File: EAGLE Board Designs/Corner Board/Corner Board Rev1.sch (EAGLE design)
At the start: 15 parts, among them J1 CONNECTOR-4_μF_T_V_BLACK, J2 CONNECTOR-2_MOLEX_NANOFIT_PTH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, J3 CONNECTOR-10_MF_T_V_, J4 CONNECTOR-4_μF_T_V_BLACK, J5 CONNECTOR-4_μF_T_V_BLACK, U1 VOLTAGE_REGULATOR_SOT-89_15V, U2 OPAMP_1_CHANNEL_OPA991, U3 INA823DT

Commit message: Update Corner Board Rev1.sch
Added MAX6176 part to Corner Board Rev1 schematic.
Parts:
- removed R3, R5: RESISTOR_0603_2K, HyTechDevices:RESISTOR_0603_2K
- added C3: CAPACITOR_0603_25V_1UF, HyTechDevices:CAPACITOR_0603_25V_1UF
- added U$6: VOLTAGE_REFERENCE__10V, temp:VOLTAGE_REFERENCE__10V
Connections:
- new net OUT: C3.1, U$6.OUT
- net +24V: now also U$6.VIN
- net GND: now also C3.2, U$6.GND
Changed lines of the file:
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@@
 <part name="P5" library="HyTechSupplies" deviceset="GND" device=""/>
 <part name="U2" library="HyTechDevices" deviceset="OPAMP_1_CHANNEL_*" device="" technology="OPA991"/>
-<part name="U$3" library="HyTechSupplies" deviceset="+24V" device=""/>
 <part name="R1" library="HyTechDevices" deviceset="RESISTOR_?_*" device="0603" technology="1K"/>
 <part name="R2" library="HyTechDevices" deviceset="RESISTOR_?_*" device="0603" technology="10K"/>
@@
 <part name="C1" library="HyTechDevices" deviceset="CAPACITOR_?_*" device="0603" technology="25V_0.1UF"/>
 <part name="U3" library="HyTechDevices" deviceset="INA823*" device="" technology="DT"/>
-<part name="R3" library="HyTechDevices" deviceset="RESISTOR_?_*" device="0603" technology="2K"/>
 <part name="R4" library="HyTechDevices" deviceset="RESISTOR_?_*" device="0603" technology="50"/>
 <part name="P8" library="HyTechSupplies" deviceset="GND" device=""/>
 <part name="U$5" library="HyTechSupplies" deviceset="+24V" device=""/>
 <part name="C2" library="HyTechDevices" deviceset="CAPACITOR_?_*" device="0603" technology="25V_0.1UF"/>
-<part name="R5" library="HyTechDevices" deviceset="RESISTOR_?_*" device="0603" technology="2K"/>
+<part name="U$3" library="HyTechSupplies" deviceset="+24V" device=""/>
 <part name="P9" library="HyTechSupplies" deviceset="GND" device=""/>
+<part name="U$6" library="temp" deviceset="VOLTAGE_REFERENCE_?_*" device="" technology="10V"/>
+<part name="C3" library="HyTechDevices" deviceset="CAPACITOR_?_*" device="0603" technology="25V_1UF"/>
 </parts>
 <sheets>
@@
 <attribute name="MPN" x="127" y="22.098" size="1.27" layer="95" align="top-left"/>
 </instance>
-<instance part="U$3" gate="G$1" x="63.5" y="-15.24" smashed="yes">
-<attribute name="VALUE" x="63.5" y="-10.16" size="1.778" layer="96" align="bottom-center"/>
-</instance>
 <instance part="R1" gate="G$1" x="121.92" y="0" smashed="yes">
 <attribute name="NAME" x="120.65" y="1.27" size="1.27" layer="95" align="bottom-center"/>
@@
 <attribute name="MPN" x="96.52" y="27.178" size="1.27" layer="95" align="top-left"/>
 </instance>
-<instance part="R3" gate="G$1" x="63.5" y="-22.86" smashed="yes" rot="R90">
-<attribute name="NAME" x="62.23" y="-24.13" size="1.27" layer="95" rot="R90" align="bottom-center"/>
-<attribute name="RESISTANCE" x="64.77" y="-24.13" size="1.27" layer="96" rot="R90" align="top-center"/>
-</instance>
 <instance part="R4" gate="G$1" x="91.44" y="12.7" smashed="yes">
 <attribute name="NAME" x="90.17" y="13.97" size="1.27" layer="95" align="bottom-center"/>
@@
 <attribute name="CAPACITANCE" x="116.078" y="34.29" size="1.27" layer="96" rot="R90" align="top-center"/>
 </instance>
-<instance part="R5" gate="G$1" x="78.74" y="-33.02" smashed="yes" rot="R90">
-<attribute name="NAME" x="77.47" y="-34.29" size="1.27" layer="95" rot="R90" align="bottom-center"/>
-<attribute name="RESISTANCE" x="80.01" y="-34.29" size="1.27" layer="96" rot="R90" align="top-center"/>
-</instance>
-<instance part="P9" gate="1" x="78.74" y="-45.72" smashed="yes">
-<attribute name="VALUE" x="78.74" y="-46.99" size="1.27" layer="96" align="top-center"/>
+<instance part="U$3" gate="G$1" x="71.12" y="-7.62" smashed="yes">
+<attribute name="VALUE" x="71.12" y="-2.54" size="1.778" layer="96" align="bottom-center"/>
+</instance>
+<instance part="P9" gate="1" x="71.12" y="-40.64" smashed="yes">
+<attribute name="VALUE" x="71.12" y="-41.91" size="1.27" layer="96" align="top-center"/>
+</instance>
+<instance part="U$6" gate="G$1" x="60.96" y="-12.7" smashed="yes">
+<attribute name="NAME" x="60.96" y="-12.7" size="1.778" layer="95"/>
+<attribute name="MPN" x="60.96" y="-31.242" size="1.778" layer="95" align="top-left"/>
+</instance>
+<instance part="C3" gate="G$1" x="88.9" y="-22.86" smashed="yes" rot="R90">
+<attribute name="NAME" x="86.36" y="-24.13" size="1.27" layer="95" rot="R90" align="bottom-center"/>
+<attribute name="VOLTAGE" x="91.44" y="-24.13" size="1.27" layer="96" rot="R90" align="top-center"/>
+<attribute name="CAPACITANCE" x="93.218" y="-24.13" size="1.27" layer="96" rot="R90" align="top-center"/>
 </instance>
 </instances>
@@
 <pinref part="U3" gate="P" pin="GND"/>
 </segment>
+<segment>
+<pinref part="U$6" gate="G$1" pin="GND"/>
+<pinref part="P9" gate="1" pin="GND"/>
+<wire x1="71.12" y1="-38.1" x2="71.12" y2="-35.56" width="0.1524" layer="91"/>
+<pinref part="C3" gate="G$1" pin="2"/>
+<wire x1="71.12" y1="-35.56" x2="71.12" y2="-33.02" width="0.1524" layer="91"/>
+<wire x1="88.9" y1="-27.94" x2="88.9" y2="-35.56" width="0.1524" layer="91"/>
+<wire x1="88.9" y1="-35.56" x2="71.12" y2="-35.56" width="0.1524" layer="91"/>
+<junction x="71.12" y="-35.56"/>
+</segment>
 </net>
 <net name="SIGNAL+" class="0">
@@
 <junction x="111.76" y="38.1"/>
 <pinref part="U3" gate="P" pin="VDD"/>
+</segment>
+<segment>
+<pinref part="U$6" gate="G$1" pin="VIN"/>
+<pinref part="U$3" gate="G$1" pin="+24V"/>
 </segment>
 </net>
@@
 </segment>
 </net>
+<net name="OUT" class="0">
+<segment>
+<pinref part="U$6" gate="G$1" pin="OUT"/>
+<pinref part="C3" gate="G$1" pin="1"/>
+<wire x1="83.82" y1="-17.78" x2="88.9" y2="-17.78" width="0.1524" layer="91"/>
+<wire x1="88.9" y1="-17.78" x2="88.9" y2="-20.32" width="0.1524" layer="91"/>
+</segment>
+</net>

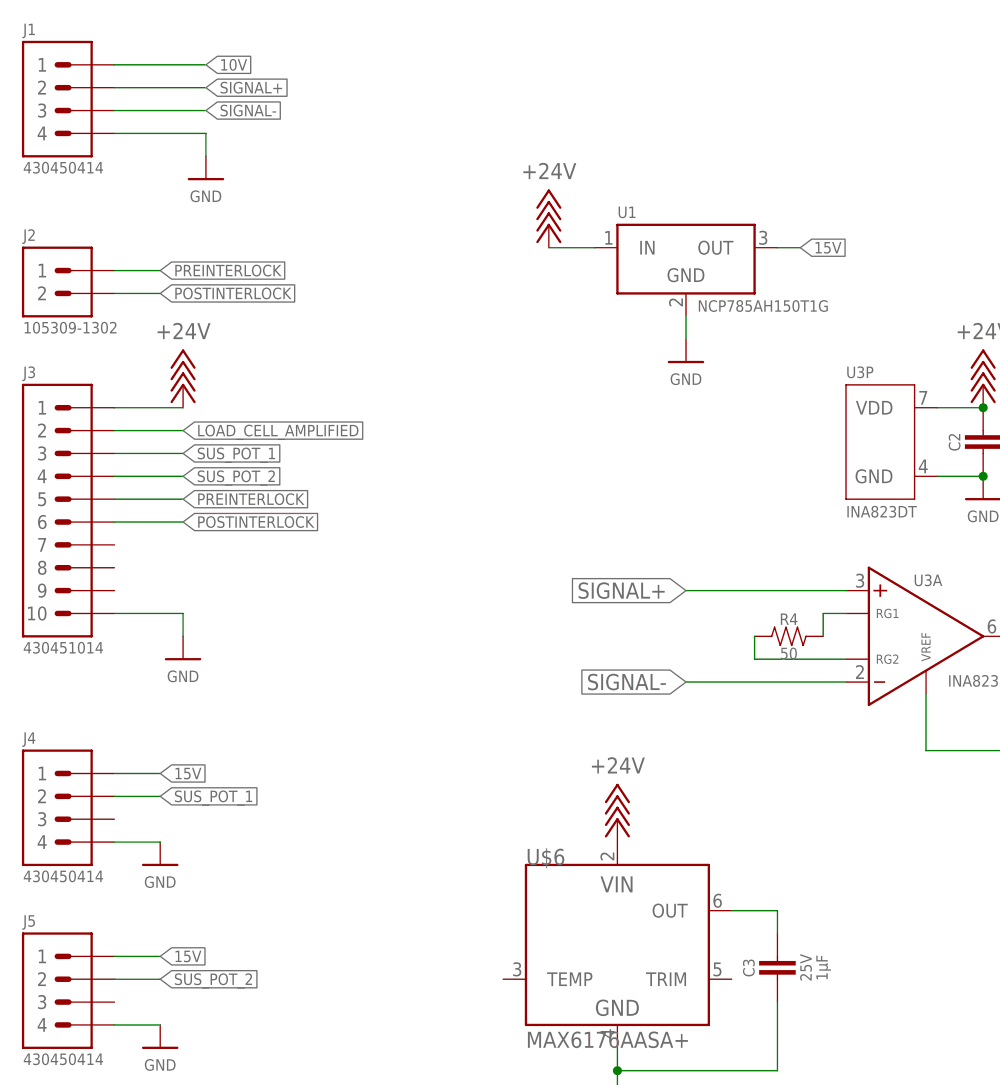
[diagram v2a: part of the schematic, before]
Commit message: updated to amphenol connectors
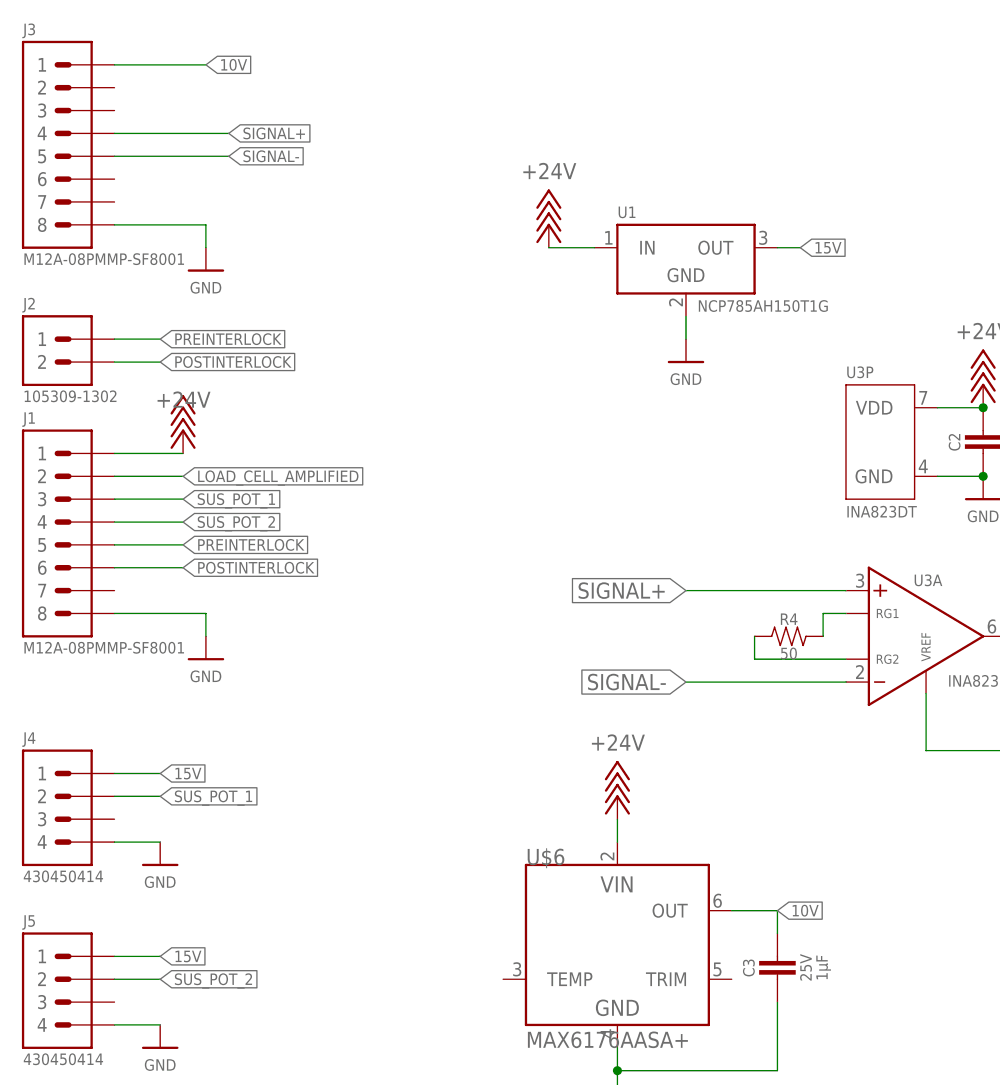
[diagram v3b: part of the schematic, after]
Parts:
- J1: value CONNECTOR-4_μF_T_V_BLACK -> CONNECTOR-8_AMPHENOL_M12A_08PMMP_; device HyTechDevices:CONNECTOR-4_μF_T_V_BLACK -> HyTechDevices:CONNECTOR-8_AMPHENOL_M12A_08PMMP_
- J3: value CONNECTOR-10_MF_T_V_ -> CONNECTOR-8_AMPHENOL_M12A_08PMMP_; device HyTechDevices:CONNECTOR-10_MF_T_V_ -> HyTechDevices:CONNECTOR-8_AMPHENOL_M12A_08PMMP_
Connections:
- removed net OUT: C3.1, U$6.OUT
- net +24V: now also J1.1; no longer J3.1
- net 10V: now also C3.1, J3.1, U$6.OUT; no longer J1.1
- net GND: now also J1.8, J3.8; no longer J1.4, J3.10
- net LOAD_CELL_AMPLIFIED: now also J1.2; no longer J3.2
- net POSTINTERLOCK: now also J1.6; no longer J3.6
- net PREINTERLOCK: now also J1.5; no longer J3.5
- net SIGNAL+: now also J3.4; no longer J1.2
- net SIGNAL-: now also J3.5; no longer J1.3
- net SUS_POT_1: now also J1.3; no longer J3.3
- net SUS_POT_2: now also J1.4; no longer J3.4
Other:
- moved on the sheet: J2

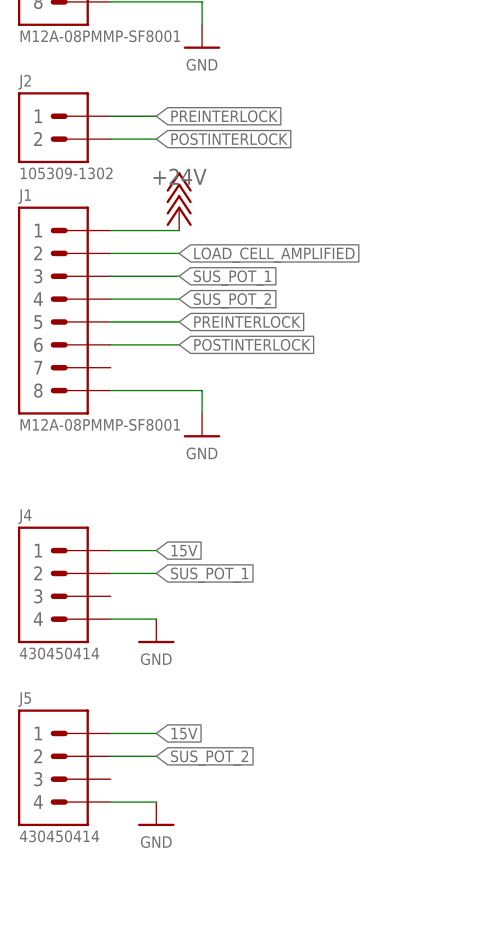
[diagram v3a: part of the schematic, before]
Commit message: preliminary placement of parts will change later
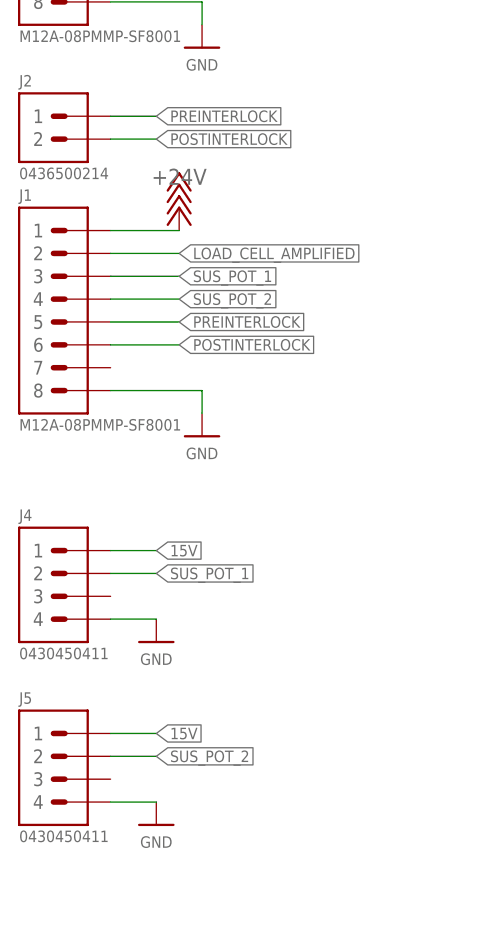
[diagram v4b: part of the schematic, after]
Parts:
- J2: value CONNECTOR-2_MOLEX_NANOFIT_PTH_VERTICAL_02_BLACK -> CONNECTOR-2_MICROFIT_SMD_RIGHTANGLE_02_SINGLE_BLACK; device HyTechDevices:CONNECTOR-2_MOLEX_NANOFIT_PTH_VERTICAL_02_BLACK -> HyTechDevices:CONNECTOR-2_MICROFIT_SMD_RIGHTANGLE_02_SINGLE_BLACK
- J4, J5: value CONNECTOR-4_μF_T_V_BLACK -> CONNECTOR-4_μF_S_RA_; device HyTechDevices:CONNECTOR-4_μF_T_V_BLACK -> HyTechDevices:CONNECTOR-4_μF_S_RA_
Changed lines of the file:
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@@
 </classes>
 <parts>
-<part name="J2" library="HyTechDevices" deviceset="CONNECTOR-2_?_*" device="MOLEX_NANOFIT_PTH_VERTICAL_02" technology="BLACK"/>
+<part name="J2" library="HyTechDevices" deviceset="CONNECTOR-2_?_*" device="MICROFIT_SMD_RIGHTANGLE_02_SINGLE" technology="BLACK" value="CONNECTOR-2_MICROFIT_SMD_RIGHTANGLE_02_SINGLE_BLACK"/>
 <part name="P1" library="HyTechSupplies" deviceset="GND" device=""/>
 <part name="U$1" library="HyTechSupplies" deviceset="+24V" device=""/>
 <part name="P2" library="HyTechSupplies" deviceset="GND" device=""/>
-<part name="J4" library="HyTechDevices" deviceset="CONNECTOR-4_?_*" device="μF_T_V" technology="BLACK"/>
-<part name="J5" library="HyTechDevices" deviceset="CONNECTOR-4_?_*" device="μF_T_V" technology="BLACK"/>
+<part name="J4" library="HyTechDevices" deviceset="CONNECTOR-4_?_*" device="μF_S_RA" value="CONNECTOR-4_μF_S_RA_"/>
+<part name="J5" library="HyTechDevices" deviceset="CONNECTOR-4_?_*" device="μF_S_RA" value="CONNECTOR-4_μF_S_RA_"/>
 <part name="P3" library="HyTechSupplies" deviceset="GND" device=""/>
 <part name="P4" library="HyTechSupplies" deviceset="GND" device=""/>

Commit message: some edits
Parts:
- added C4, C5: CAPACITOR_0603_25V_0.1UF, HyTechDevices:CAPACITOR_0603_25V_0.1UF
- added R3, R7: RESISTOR_0603_10K, HyTechDevices:RESISTOR_0603_10K
- added R5, R8: RESISTOR_0603_2.74K, HyTechDevices:RESISTOR_0603_2.74K
- added R6, R9: RESISTOR_0603_10.5K, HyTechDevices:RESISTOR_0603_10.5K
- added U4, U5: OPAMP_1_CHANNEL_OPA991, HyTechDevices:OPAMP_1_CHANNEL_OPA991
- R4: value RESISTOR_0603_50 -> RESISTOR_0603_2.74K; device HyTechDevices:RESISTOR_0603_50 -> HyTechDevices:RESISTOR_0603_2.74K
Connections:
- new net N$5: R5.2, R6.1, U4A.VIN-
- new net N$7: R7.1, R8.1
- new net N$8: R8.2, R9.1, U5A.VIN-
- new net SUS_POT_1_24V: J1.3, R9.2, U5A.VOUT
- new net SUS_POT_2_24V: J1.4, R6.2, U4A.VOUT
- net +24V: now also C4.1, C5.1, U4P.VDD, U5P.VDD
- net GND: now also C4.2, C5.2, R3.1, R5.1, U4P.GND, U5P.GND
- net SUS_POT_1: now also R7.2, U5A.VIN+; no longer J1.3
- net SUS_POT_2: now also R3.2, U4A.VIN+; no longer J1.4

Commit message: design review changes
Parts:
- renumbered U$6 to U6
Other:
- moved on the sheet: R3, R5, R6, R7, R8, R9, U4A, U5A

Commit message: design review changes
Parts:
- R2: value RESISTOR_0603_10K -> RESISTOR_0603_22.1K; device HyTechDevices:RESISTOR_0603_10K -> HyTechDevices:RESISTOR_0603_22.1K
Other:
- note added: "23.1x gain"
- note added: "37.5x gain"
- note added: "5V -> 24.16V 4.832x gain"
- note added: "866.3x gain total"
- moved on the sheet: R1, R2
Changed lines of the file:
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@@
 <part name="U2" library="HyTechDevices" deviceset="OPAMP_1_CHANNEL_*" device="" technology="OPA991"/>
 <part name="R1" library="HyTechDevices" deviceset="RESISTOR_?_*" device="0603" technology="1K"/>
-<part name="R2" library="HyTechDevices" deviceset="RESISTOR_?_*" device="0603" technology="10K"/>
+<part name="R2" library="HyTechDevices" deviceset="RESISTOR_?_*" device="0603" technology="22.1K" value="RESISTOR_0603_22.1K"/>
 <part name="P6" library="HyTechSupplies" deviceset="GND" device=""/>
 <part name="P7" library="HyTechSupplies" deviceset="GND" device=""/>
@@
 <sheet>
 <plain>
+<text x="73.66" y="-86.36" size="1.27" layer="97">5V -&gt; 24.16V
+4.832x gain</text>
+<text x="76.2" y="-53.34" size="1.27" layer="97">5V -&gt; 24.16V
+4.832x gain</text>
+<text x="111.76" y="17.78" size="1.27" layer="97">37.5x gain</text>
+<text x="142.24" y="12.7" size="1.27" layer="97">23.1x gain</text>
+<text x="154.94" y="2.54" size="1.27" layer="97">866.3x gain total</text>
 </plain>
 <instances>
@@
 <attribute name="MPN" x="127" y="22.098" size="1.27" layer="95" align="top-left"/>
 </instance>
-<instance part="R1" gate="G$1" x="121.92" y="0" smashed="yes">
-<attribute name="NAME" x="120.65" y="1.27" size="1.27" layer="95" align="bottom-center"/>
-<attribute name="RESISTANCE" x="120.65" y="-1.27" size="1.27" layer="96" align="top-center"/>
-</instance>
-<instance part="R2" gate="G$1" x="139.7" y="0" smashed="yes">
-<attribute name="NAME" x="138.43" y="1.27" size="1.27" layer="95" align="bottom-center"/>
-<attribute name="RESISTANCE" x="138.43" y="-1.27" size="1.27" layer="96" align="top-center"/>
+<instance part="R1" gate="G$1" x="124.46" y="0" smashed="yes">
+<attribute name="NAME" x="123.19" y="1.27" size="1.27" layer="95" align="bottom-center"/>
+<attribute name="RESISTANCE" x="123.19" y="-1.27" size="1.27" layer="96" align="top-center"/>
+</instance>
+<instance part="R2" gate="G$1" x="137.16" y="0" smashed="yes">
+<attribute name="NAME" x="135.89" y="1.27" size="1.27" layer="95" align="bottom-center"/>
+<attribute name="RESISTANCE" x="135.89" y="-1.27" size="1.27" layer="96" align="top-center"/>
 </instance>
 <instance part="P6" gate="1" x="116.84" y="-10.16" smashed="yes">
@@
 <wire x1="78.74" y1="48.26" x2="78.74" y2="45.72" width="0.1524" layer="91"/>
 <pinref part="P5" gate="1" pin="GND"/>
-</segment>
-<segment>
-<pinref part="R1" gate="G$1" pin="1"/>
-<wire x1="116.84" y1="0" x2="116.84" y2="-7.62" width="0.1524" layer="91"/>
-<pinref part="P6" gate="1" pin="GND"/>
-<pinref part="U3" gate="A" pin="VREF"/>
-<wire x1="105.41" y1="6.35" x2="105.41" y2="0" width="0.1524" layer="91"/>
-<wire x1="105.41" y1="0" x2="116.84" y2="0" width="0.1524" layer="91"/>
-<junction x="116.84" y="0"/>
 </segment>
 <segment>
@@
 <junction x="22.86" y="-66.04"/>
 </segment>
+<segment>
+<pinref part="R1" gate="G$1" pin="1"/>
+<pinref part="U3" gate="A" pin="VREF"/>
+<wire x1="105.41" y1="6.35" x2="105.41" y2="0" width="0.1524" layer="91"/>
+<wire x1="105.41" y1="0" x2="116.84" y2="0" width="0.1524" layer="91"/>
+<pinref part="P6" gate="1" pin="GND"/>
+<wire x1="116.84" y1="0" x2="119.38" y2="0" width="0.1524" layer="91"/>
+<wire x1="116.84" y1="-7.62" x2="116.84" y2="0" width="0.1524" layer="91"/>
+<junction x="116.84" y="0"/>
+</segment>
 </net>
 <net name="SIGNAL+" class="0">
@@
 <segment>
 <pinref part="U2" gate="A" pin="VOUT"/>
-<wire x1="139.7" y1="10.16" x2="142.24" y2="10.16" width="0.1524" layer="91"/>
 <label x="147.32" y="10.16" size="1.27" layer="95" xref="yes"/>
+<wire x1="147.32" y1="10.16" x2="142.24" y2="10.16" width="0.1524" layer="91"/>
 <pinref part="R2" gate="G$1" pin="2"/>
-<wire x1="144.78" y1="10.16" x2="147.32" y2="10.16" width="0.1524" layer="91"/>
-<wire x1="144.78" y1="10.16" x2="142.24" y2="10.16" width="0.1524" layer="91"/>
-<wire x1="142.24" y1="10.16" x2="142.24" y2="0" width="0.1524" layer="91"/>
+<wire x1="142.24" y1="10.16" x2="139.7" y2="10.16" width="0.1524" layer="91"/>
+<wire x1="139.7" y1="0" x2="142.24" y2="0" width="0.1524" layer="91"/>
+<wire x1="142.24" y1="0" x2="142.24" y2="10.16" width="0.1524" layer="91"/>
+<junction x="142.24" y="10.16"/>
 </segment>
 </net>
@@
 <wire x1="129.54" y1="7.62" x2="129.54" y2="0" width="0.1524" layer="91"/>
 <pinref part="R2" gate="G$1" pin="1"/>
-<wire x1="129.54" y1="0" x2="134.62" y2="0" width="0.1524" layer="91"/>
+<wire x1="129.54" y1="0" x2="132.08" y2="0" width="0.1524" layer="91"/>
 <pinref part="R1" gate="G$1" pin="2"/>
-<wire x1="129.54" y1="0" x2="124.46" y2="0" width="0.1524" layer="91"/>
+<wire x1="129.54" y1="0" x2="127" y2="0" width="0.1524" layer="91"/>
 <junction x="129.54" y="0"/>
 </segment>
